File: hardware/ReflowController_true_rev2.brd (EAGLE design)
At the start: 80 x 50 mm, 46 parts, among them IC1 MAX31855, IC2 MAX31855

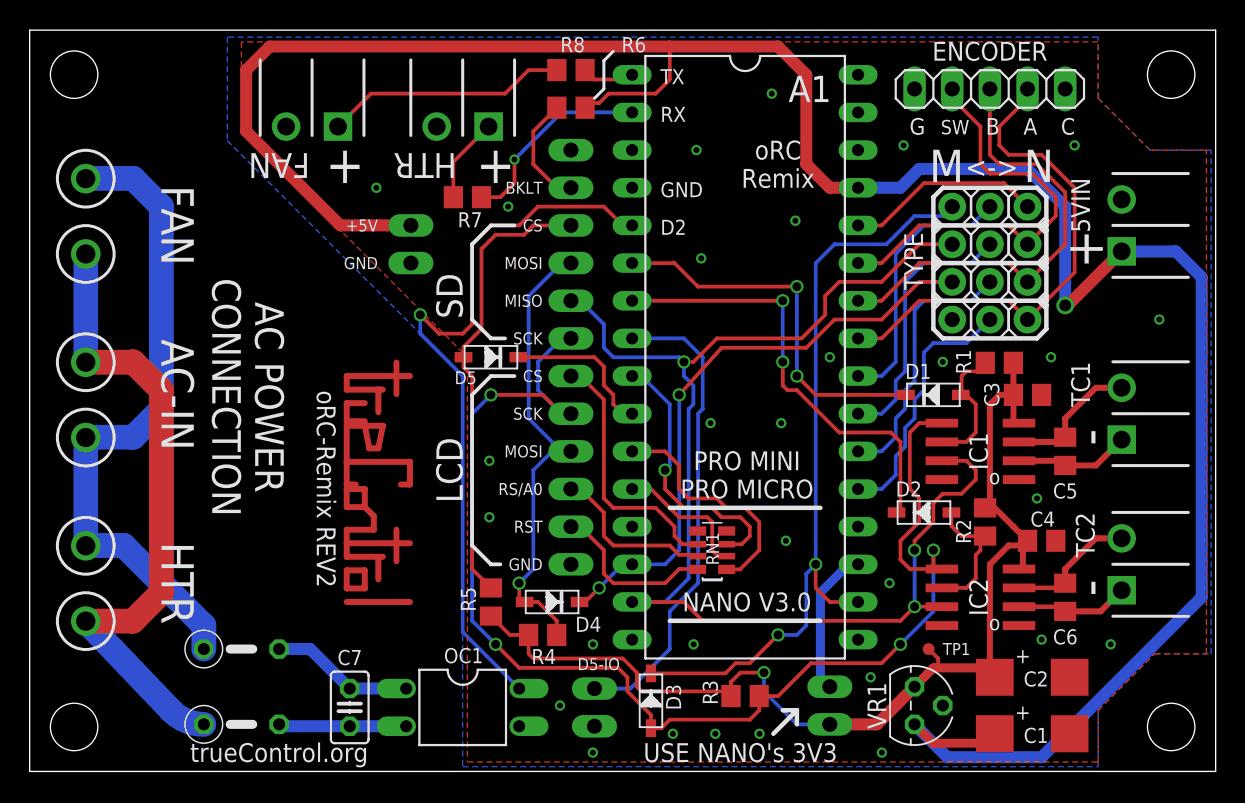
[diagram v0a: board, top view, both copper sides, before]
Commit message: Board: Fixed C7 mains cap size
Changed C7 cap to a standard 15mm width X2 cap. Reworked the board in
this area to get it to fit.
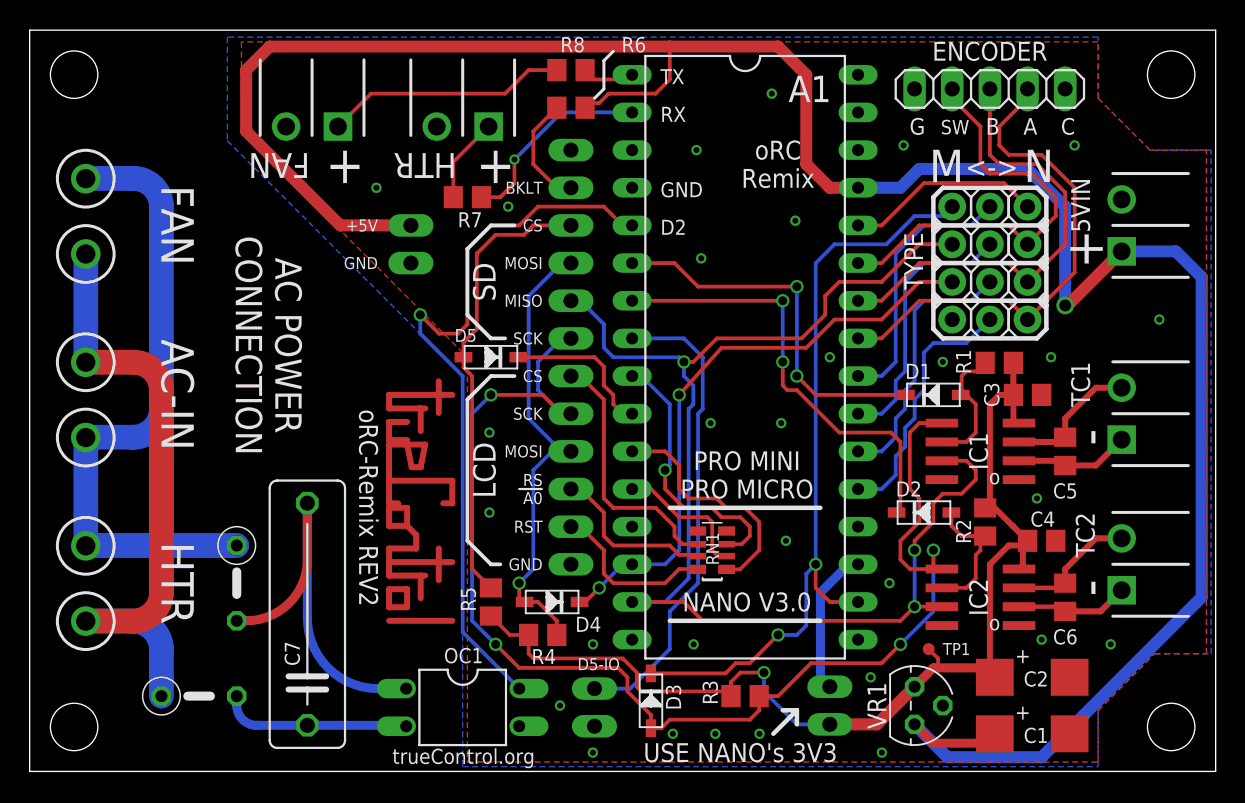
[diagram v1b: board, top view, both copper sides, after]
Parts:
- C7: device rcl:C025-025X050 -> rcl:C150-054X183
- moved C7 6.91 mm to (18.7, 10.6), turned to 90 degrees
- moved R9 4.46 mm to (14.0, 12.7), turned to 270 degrees
- moved R10 3.43 mm to (11.4, 5.08)
- moved U$1 3.13 mm to (24.4, 25.4)
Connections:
- removed net N$10: C7.2, OC1.2, R10.2
- new net N$6: C7.2, OC1.1, R9.2
- net N$9: now also OC1.2, R10.2; no longer OC1.1, R9.2
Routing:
- net N$6: track 0.00 -> 26.7 mm
- net N$10: track 8.99 -> 0.00 mm
- net N$9: track 9.68 -> 12.6 mm
- net AC2: track 43.5 -> 41.8 mm
- net AC1: track 44.5 -> 42.9 mm
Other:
- board text added: "RS A0"
- board text removed: "RS/A0"
